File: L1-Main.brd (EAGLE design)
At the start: 19 parts

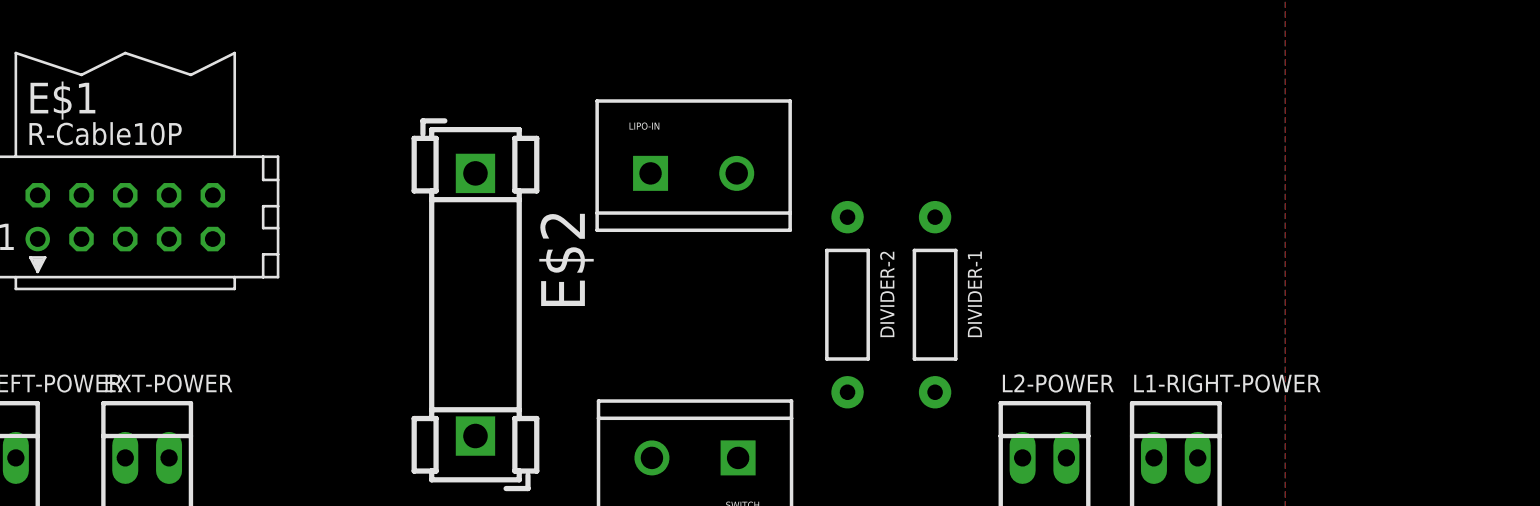
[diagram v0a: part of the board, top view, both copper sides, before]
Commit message: All boards defined
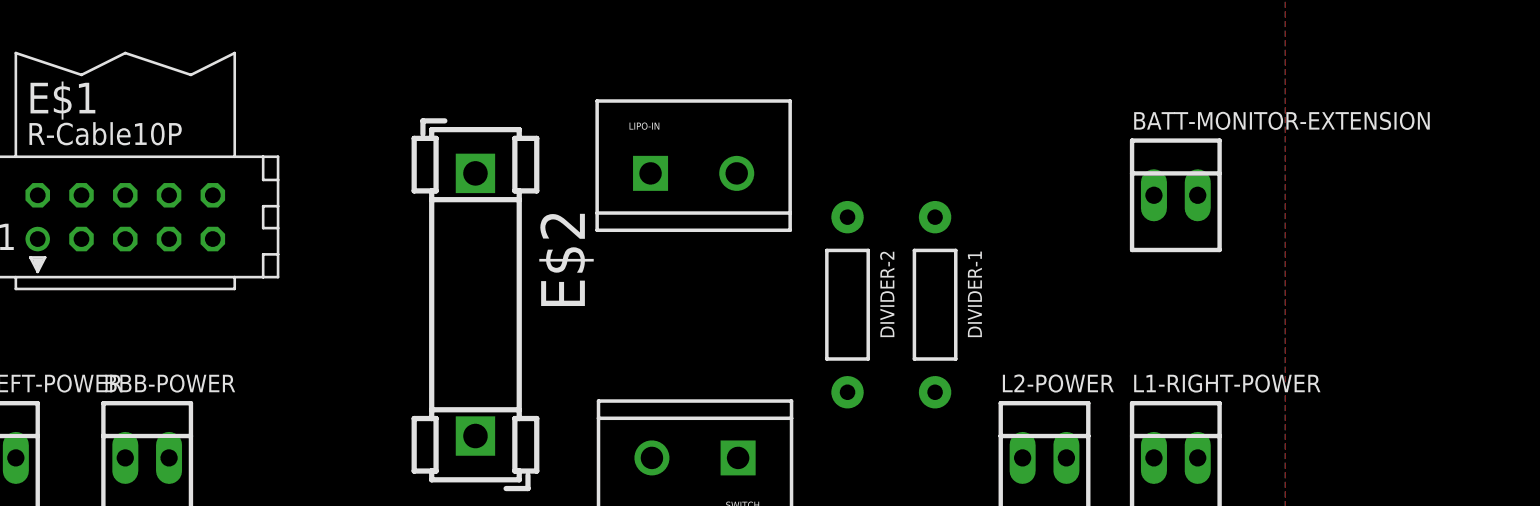
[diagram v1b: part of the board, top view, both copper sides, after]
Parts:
- added BATT-MONITOR-EXTENSION: (no value), con-molex:22-23-2021
- renumbered EXT-POWER to BBB-POWER
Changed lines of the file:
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@@
 <board>
 <plain>
-<dimension x1="0" y1="0" x2="80.01" y2="0" x3="40.005" y3="-11.43" textsize="1.778" layer="1" dtype="horizontal"/>
+<dimension x1="-1.27" y1="119.38" x2="10.71115625" y2="119.38" x3="5.08" y3="129.54" textsize="1.778" layer="20" dtype="angle"/>
+<dimension x1="-5.08" y1="139.7" x2="-2.54" y2="119.38" x3="-3.81" y3="143.51" textsize="1.778" layer="20" dtype="horizontal"/>
+<dimension x1="-5.08" y1="139.7" x2="15.24" y2="123.19" x3="5.08" y3="147.32" textsize="1.778" layer="20" dtype="horizontal"/>
+<dimension x1="15.24" y1="120.65" x2="35.56" y2="120.65" x3="25.4" y3="116.84" textsize="1.778" layer="20" dtype="horizontal"/>
+<dimension x1="85.09" y1="139.7" x2="39.37" y2="139.7" x3="62.23" y3="147.32" textsize="1.778" layer="20" dtype="horizontal"/>
+<dimension x1="74.93" y1="109.22" x2="85.09" y2="109.22" x3="80.01" y3="142.24" textsize="1.778" layer="20" dtype="horizontal"/>
+<dimension x1="0" y1="0" x2="80.01" y2="0" x3="40.005" y3="-6.35" textsize="1.778" layer="20" dtype="horizontal"/>
 </plain>
 <attributes>
@@
 <element name="DIVIDER-1" library="SparkFun-Passives" package="AXIAL-0.4" value="" x="59.69" y="13.97" rot="R270"/>
 <element name="DIVIDER-2" library="SparkFun-Passives" package="AXIAL-0.4" value="" x="54.61" y="13.97" rot="R270"/>
-<element name="EXT-POWER" library="con-molex" package="22-23-2021" value="" x="13.97" y="5.08"/>
+<element name="BBB-POWER" library="con-molex" package="22-23-2021" value="" x="13.97" y="5.08"/>
 <element name="L2-POWER" library="con-molex" package="22-23-2021" value="" x="66.04" y="5.08"/>
 <element name="L1-LEFT-POWER" library="con-molex" package="22-23-2021" value="" x="5.08" y="5.08"/>
 <element name="L1-RIGHT-POWER" library="con-molex" package="22-23-2021" value="" x="73.66" y="5.08"/>
 <element name="E$1" library="con-harting" package="CON10" value="" x="12.7" y="19.05"/>
+<element name="BATT-MONITOR-EXTENSION" library="con-molex" package="22-23-2021" value="" x="73.66" y="20.32"/>
 </elements>
 <signals>
